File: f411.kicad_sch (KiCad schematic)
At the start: 19 parts, among them J18 Conn_02x04_Top_Bottom, SW1 SW_Push, SW2 SW_Push, U5 STM32F411CEU6

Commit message: ongoing add of MCU, etc.
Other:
- title: ADCs for 10K thermistors -> Multiplex I2C to Screw Terminal connectors

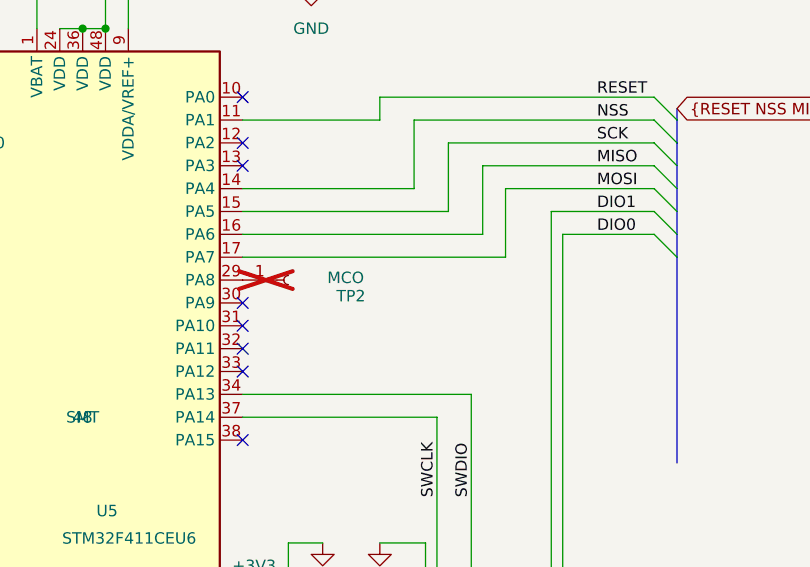
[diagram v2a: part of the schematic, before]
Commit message: symbols an footprints added for f411 change. ERC passes.
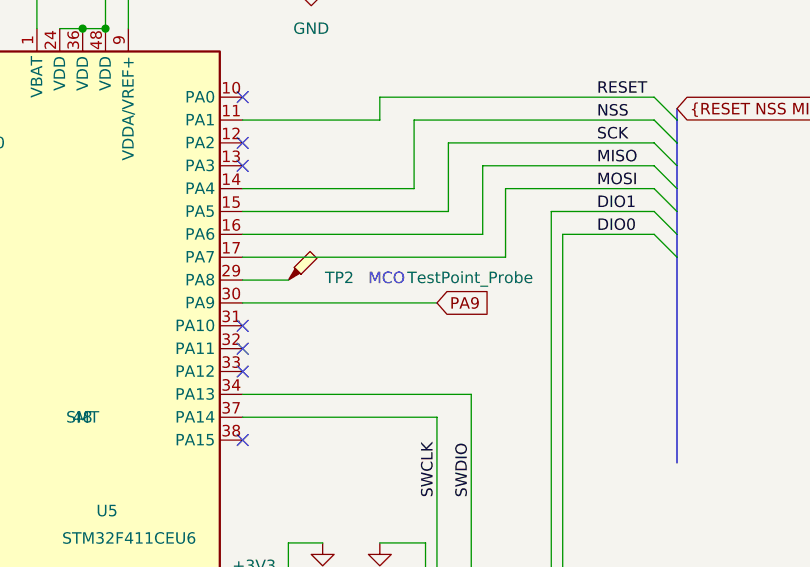
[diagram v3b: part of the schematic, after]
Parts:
- removed TP2: MCO, ProjectLib:TestPoint_Pad_D1.0mm, symbol ProjectLib:Conn_01x01_Socket
- added TP2: TestPoint_Probe, ProjectLib:TestPoint_THTPad_D1.0mm_Drill0.5mm, symbol ProjectLib:TestPoint_Probe
- C14, C17, C9: footprint ProjectLib:C_0402_1005Metric -> ProjectLib:C_0805_2012Metric
- R23, R24, R25, R26, R27, R33, R34: footprint ProjectLib:R_0402_1005Metric -> ProjectLib:R_0603_1608Metric
- U5: footprint ProjectLib:QFN-48-1EP_7x7mm_P0.5mm_EP5.6x5.6mm -> Package_DFN_QFN:QFN-48-1EP_7x7mm_P0.5mm_EP5.6x5.6mm
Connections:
- net at U5.29 (PA8): now also TP2.1
- net PA9: now reaches U5.30 (PA9)
- no-connect marks 16 -> 15
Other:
- note added: "MCO"

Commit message: ongoing
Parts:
- C14, C17, C9: footprint ProjectLib:C_0805_2012Metric -> ProjectLib:C_0402_1005Metric
- R23, R24, R25, R26, R27, R33, R34: footprint ProjectLib:R_0603_1608Metric -> ProjectLib:R_0402_1005Metric
- TP2: footprint ProjectLib:TestPoint_THTPad_D1.0mm_Drill0.5mm -> ProjectLib:TestPoint_Pad_D1.0mm; MountType (none) -> SMT
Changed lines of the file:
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@@
 			)
 		)
-		(property "Footprint" "ProjectLib:R_0603_1608Metric"
+		(property "Footprint" "ProjectLib:R_0402_1005Metric"
 			(at 62.992 63.5 90)
 			(effects
@@
 			)
 		)
-		(property "Footprint" "ProjectLib:TestPoint_THTPad_D1.0mm_Drill0.5mm"
+		(property "Footprint" "ProjectLib:TestPoint_Pad_D1.0mm"
 			(at 172.72 87.63 0)
 			(effects
@@
 			)
 		)
+		(property "MountType" "SMT"
+			(at 167.64 87.63 0)
+			(effects
+				(font
+					(size 1.27 1.27)
+				)
+				(hide yes)
+			)
+		)
 		(pin "1"
 		)
@@
 			)
 		)
-		(property "Footprint" "ProjectLib:R_0603_1608Metric"
+		(property "Footprint" "ProjectLib:R_0402_1005Metric"
 			(at 185.674 152.654 90)
 			(effects
@@
 			)
 		)
-		(property "Footprint" "ProjectLib:C_0805_2012Metric"
+		(property "Footprint" "ProjectLib:C_0402_1005Metric"
 			(at 124.1552 143.51 0)
 			(effects
@@
 			)
 		)
-		(property "Footprint" "ProjectLib:R_0603_1608Metric"
+		(property "Footprint" "ProjectLib:R_0402_1005Metric"
 			(at 94.742 109.22 90)
 			(effects
@@
 			)
 		)
-		(property "Footprint" "ProjectLib:C_0805_2012Metric"
+		(property "Footprint" "ProjectLib:C_0402_1005Metric"
 			(at 71.12 43.4848 0)
 			(effects
@@
 			)
 		)
-		(property "Footprint" "ProjectLib:C_0805_2012Metric"
+		(property "Footprint" "ProjectLib:C_0402_1005Metric"
 			(at 171.1452 54.61 0)
 			(effects
@@
 			)
 		)
-		(property "Footprint" "ProjectLib:R_0603_1608Metric"
+		(property "Footprint" "ProjectLib:R_0402_1005Metric"
 			(at 92.202 40.64 90)
 			(effects
@@
 			)
 		)
-		(property "Footprint" "ProjectLib:R_0603_1608Metric"
+		(property "Footprint" "ProjectLib:R_0402_1005Metric"
 			(at 189.484 141.224 90)
 			(effects
@@
 			)
 		)
-		(property "Footprint" "ProjectLib:R_0603_1608Metric"
+		(property "Footprint" "ProjectLib:R_0402_1005Metric"
 			(at 62.23 86.868 90)
 			(effects
@@
 			)
 		)
-		(property "Footprint" "ProjectLib:R_0603_1608Metric"
+		(property "Footprint" "ProjectLib:R_0402_1005Metric"
 			(at 40.132 80.01 90)
 			(effects

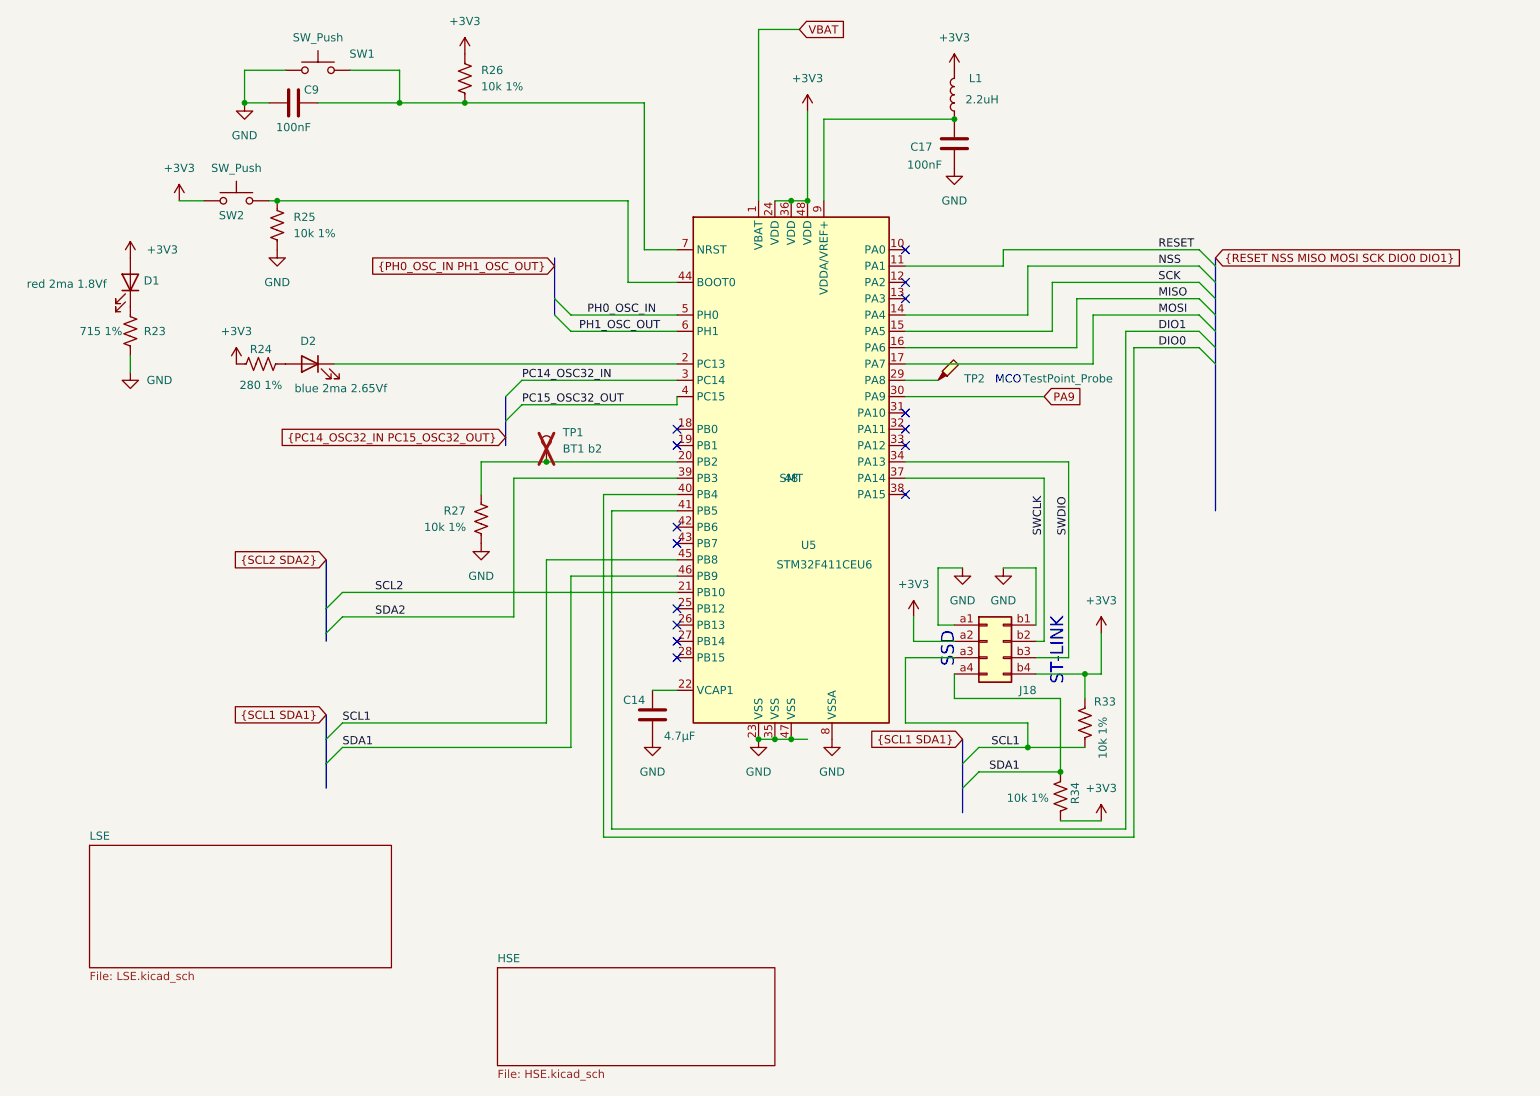
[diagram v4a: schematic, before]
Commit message: adding MCU, ongoing.
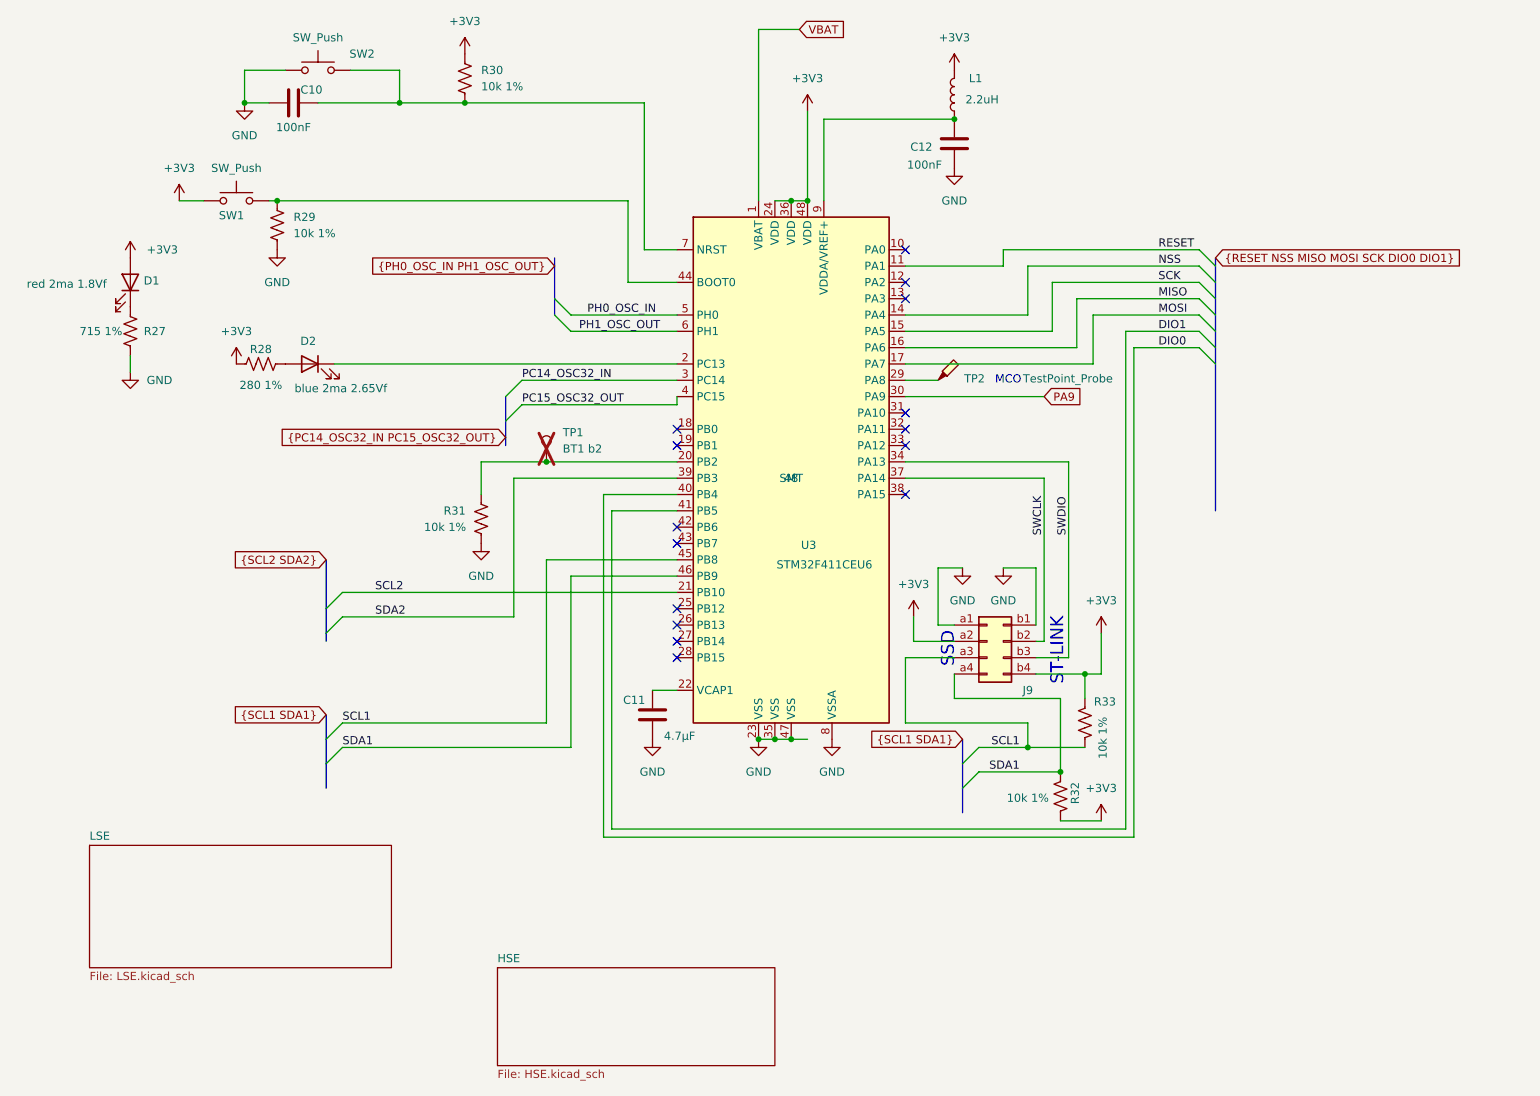
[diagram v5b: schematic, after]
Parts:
- renumbered C9 to C10, C14 to C11, C17 to C12, J18 to J9, R23 to R27, R24 to R28, R25 to R29, R26 to R30, R27 to R31, R34 to R32, SW2 to SW1, SW1 to SW2, U5 to U3

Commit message: th8-f411 with castellated MCU-LoRa. DRC clean, ERC with some warnings.
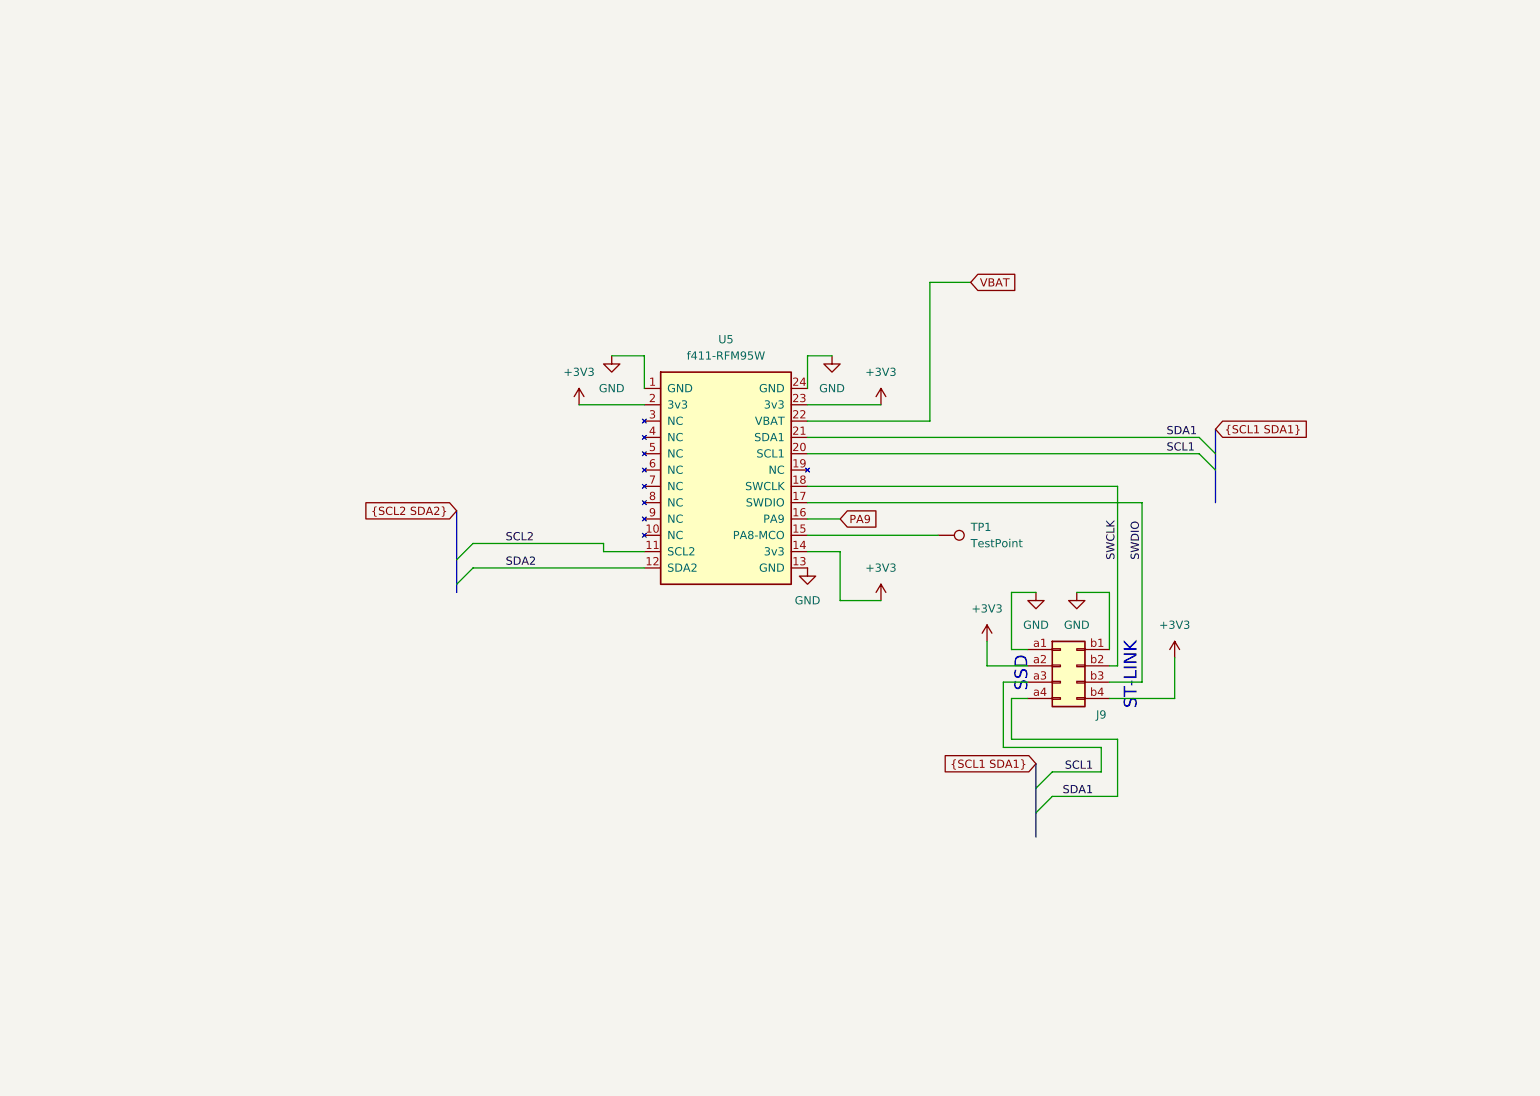
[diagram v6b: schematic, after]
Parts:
- removed C10, C12: 100nF, ProjectLib:C_0402_1005Metric, symbol ProjectLib:C
- removed C11: 4.7µF, ProjectLib:C_0402_1005Metric, symbol ProjectLib:C
- removed D1: red 2ma 1.8Vf, ProjectLib:LED_0603_1608Metric, symbol ProjectLib:LED
- removed D2: blue 2ma 2.65Vf, ProjectLib:LED_0603_1608Metric, symbol ProjectLib:LED
- removed L1: 2.2uH, ProjectLib:L_0402_1005Metric, symbol ProjectLib:L
- removed R27: 715 1%, ProjectLib:R_0402_1005Metric, symbol ProjectLib:R_US
- removed R28: 280 1%, ProjectLib:R_0402_1005Metric, symbol ProjectLib:R_US
- removed R29, R30, R31, R32, R33: 10k 1%, ProjectLib:R_0402_1005Metric, symbol ProjectLib:R_US
- removed SW1, SW2: SW_Push, ProjectLib:SW_SPST_B3U-1000P, symbol ProjectLib:SW_Push
- removed TP1: BT1 b2, ProjectLib:TestPoint_Pad_D1.0mm, symbol ProjectLib:TestPoint
- removed TP2: TestPoint_Probe, ProjectLib:TestPoint_Pad_D1.0mm, symbol ProjectLib:TestPoint_Probe
- removed U3: STM32F411CEU6, Package_DFN_QFN:QFN-48-1EP_7x7mm_P0.5mm_EP5.6x5.6mm, symbol ProjectLib:STM32F411CEUx
- added TP1: TestPoint, ProjectLib:TestPoint_Pad_D1.0mm, symbol MySymbols:TestPoint
- added U5: f411-RFM95W, ProjectLib:Castellated_MCU-LoRa_20x50mm_2x12_P2.0mm_SMD, symbol MySymbol_Library:f411-RFM95
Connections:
- net +3V3: now also U5.14 (3v3), U5.2 (3v3), U5.23 (3v3)
- net GND: now also U5.1 (GND), U5.13 (GND), U5.24 (GND)
- net PA9: now also U5.16 (PA9)
- net SCL1: now also U5.20 (SCL1)
- net SCL2: now also U5.11 (SCL2)
- net SDA1: now also U5.21 (SDA1)
- net SDA2: now also U5.12 (SDA2)
- net SWCLK: now also U5.18 (SWCLK)
- net SWDIO: now also U5.17 (SWDIO)
- net VBAT: now also U5.22 (VBAT)
- new net: TP1.1, U5.15 (PA8-MCO)
- no-connect marks 15 -> 0
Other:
- removed sheet HSE
- removed sheet LSE
- note removed: "MCO"
- moved on the sheet: J9

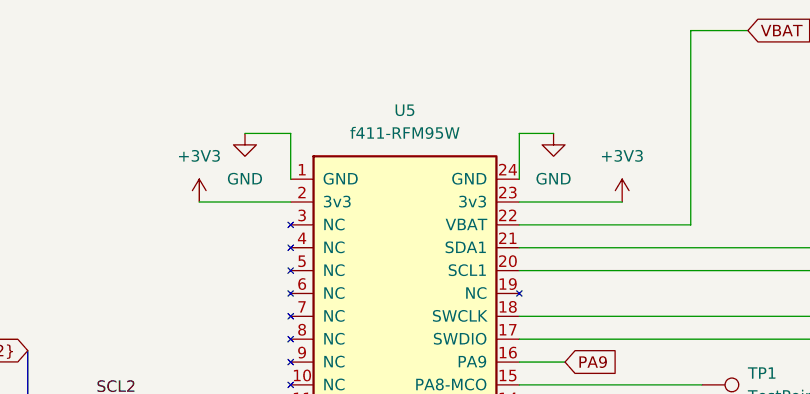
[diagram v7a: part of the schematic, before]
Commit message: changed single 10k pull-up to 4.7k like others. Renumbered components to fill numbering gaps.
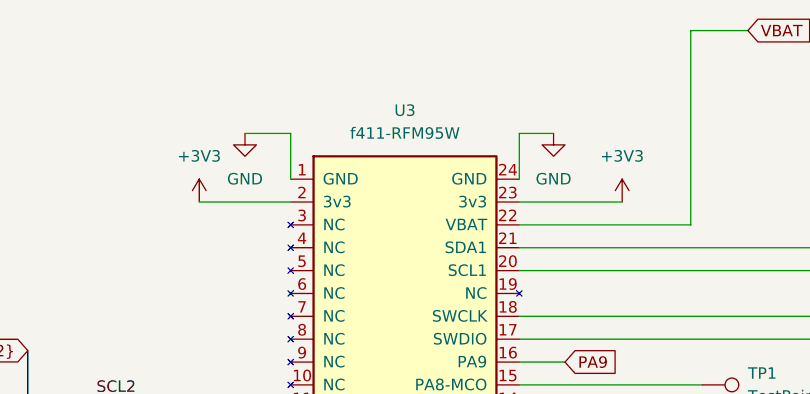
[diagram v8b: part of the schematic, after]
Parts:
- renumbered U5 to U3
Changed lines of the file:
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@@
 		(dnp no)
 		(fields_autoplaced yes)
-		(property "Reference" "U5"
+		(property "Reference" "U3"
 			(at 134.62 81.28 0)
 			(effects
@@
 			(project ""
 				(path "/0c2d0c14-8850-4a30-bb78-b2f40cb442ba/2810e5bd-88e3-445e-9497-ea39bfab4c18"
-					(reference "U5")
+					(reference "U3")
 					(unit 1)
 				)
